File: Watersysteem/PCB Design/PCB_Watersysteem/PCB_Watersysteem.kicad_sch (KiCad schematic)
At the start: 69 parts, among them J1 12V ingang, J10 LED Water Level, J11 LED Nutrient Level, J12 Height Nutrients, J13 Height Mixer, J2 TTL Connector, J23 ReferentieProbe, J24 Voedingsstoffen 1, J25 Voedingsstoffen 2, J26 Voedingsstoffen 3, J6 Height Water, J7 Endstop Lade0, J8 Endstop Lade1, J9 Endstop UV, SW1 EN, SW2 BOOT, U1 ESP32-WROOM-32D, U2 MP1584_Module, U3 AMS1117-3.3, U4 ADS1115IDGS, U5 MCP23017_SO

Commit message: Update PCB
Alle connecties gemaakt
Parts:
- removed TP5, TP6: TestPoint, TestPoint:TestPoint_Pad_D2.5mm, symbol Connector:TestPoint
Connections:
- net Nutr1: now also U4.4 (AIN0); no longer U4.5 (AIN1)
- net Nutr2: now also U4.5 (AIN1); no longer U4.6 (AIN2)
- net Nutr3: now also U4.6 (AIN2); no longer U4.7 (AIN3)
- net RELAY_AIR: now also U5.25 (GPA4); no longer U5.26 (GPA5)
- net RELAY_UV: now also U5.26 (GPA5); no longer U5.25 (GPA4)
- net Nutr0 renamed RefProbe
- net RefProbe: now also U4.7 (AIN3); no longer U4.4 (AIN0)
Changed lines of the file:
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@@
 	)
 	(junction
-		(at 74.93 177.8)
-		(diameter 0)
-		(color 0 0 0 0)
-	)
-	(junction
 		(at 92.71 133.35)
 		(diameter 0)
@@
 	)
 	(junction
-		(at 38.1 177.8)
-		(diameter 0)
-		(color 0 0 0 0)
-	)
-	(junction
 		(at 96.52 143.51)
 		(diameter 0)
@@
 	(wire
 		(pts
-			(xy 74.93 177.8) (xy 77.47 177.8)
-		)
-		(stroke
-			(width 0)
-			(type default)
-		)
-	)
-	(wire
-		(pts
 			(xy 82.55 177.8) (xy 77.47 177.8)
 		)
@@
 	(wire
 		(pts
-			(xy 33.02 177.8) (xy 38.1 177.8)
-		)
-		(stroke
-			(width 0)
-			(type default)
-		)
-	)
-	(wire
-		(pts
 			(xy 234.95 123.19) (xy 250.19 123.19)
 		)
@@
 	(wire
 		(pts
-			(xy 38.1 177.8) (xy 44.45 177.8)
+			(xy 33.02 177.8) (xy 44.45 177.8)
 		)
 		(stroke
@@
 	(wire
 		(pts
-			(xy 72.39 177.8) (xy 74.93 177.8)
+			(xy 72.39 177.8) (xy 77.47 177.8)
 		)
 		(stroke
@@
 	(global_label "Nutr2"
 		(shape input)
-		(at 241.3 59.69 180)
+		(at 241.3 57.15 180)
 		(fields_autoplaced yes)
 		(effects
@@
 		)
 		(property "Intersheetrefs" "${INTERSHEET_REFS}"
-			(at 233.1139 59.69 0)
+			(at 233.1139 57.15 0)
 			(effects
 				(font
@@
 	(global_label "Nutr3"
 		(shape input)
-		(at 241.3 62.23 180)
+		(at 241.3 59.69 180)
 		(fields_autoplaced yes)
 		(effects
@@
 		)
 		(property "Intersheetrefs" "${INTERSHEET_REFS}"
-			(at 233.1139 62.23 0)
+			(at 233.1139 59.69 0)
 			(effects
 				(font
@@
 		)
 	)
-	(global_label "Nutr0"
+	(global_label "RefProbe"
 		(shape input)
-		(at 241.3 54.61 180)
+		(at 241.3 62.23 180)
 		(fields_autoplaced yes)
 		(effects
@@
 		)
 		(property "Intersheetrefs" "${INTERSHEET_REFS}"
-			(at 233.1139 54.61 0)
+			(at 229.7877 62.23 0)
 			(effects
 				(font
@@
 	(global_label "RELAY_AIR"
 		(shape input)
-		(at 139.7 140.97 0)
+		(at 139.7 138.43 0)
 		(fields_autoplaced yes)
 		(effects
@@
 		)
 		(property "Intersheetrefs" "${INTERSHEET_REFS}"
-			(at 152.2405 140.97 0)
+			(at 152.2405 138.43 0)
 			(effects
 				(font
@@
 		)
 	)
-	(global_label "Nutr0"
+	(global_label "RefProbe"
 		(shape input)
 		(at 190.5 50.8 0)
@@
 		)
 		(property "Intersheetrefs" "${INTERSHEET_REFS}"
-			(at 198.6861 50.8 0)
+			(at 202.0123 50.8 0)
 			(effects
 				(font
@@
 	(global_label "RELAY_UV"
 		(shape input)
-		(at 139.7 138.43 0)
+		(at 139.7 140.97 0)
 		(fields_autoplaced yes)
 		(effects
@@
 		)
 		(property "Intersheetrefs" "${INTERSHEET_REFS}"
-			(at 151.6962 138.43 0)
+			(at 151.6962 140.97 0)
 			(effects
 				(font
@@
 	(global_label "Nutr1"
 		(shape input)
-		(at 241.3 57.15 180)
+		(at 241.3 54.61 180)
 		(fields_autoplaced yes)
 		(effects
@@
 		)
 		(property "Intersheetrefs" "${INTERSHEET_REFS}"
-			(at 233.1139 57.15 0)
+			(at 233.1139 54.61 0)
 			(effects
 				(font
@@
 	)
 	(symbol
-		(lib_id "Connector:TestPoint")
-		(at 38.1 177.8 0)
-		(unit 1)
-		(exclude_from_sim no)
-		(in_bom yes)
-		(on_board yes)
-		(dnp no)
-		(fields_autoplaced yes)
-		(property "Reference" "TP5"
-			(at 40.64 173.2279 0)
-			(effects
-				(font
-					(size 1.27 1.27)
-				)
-				(justify left)
-			)
-		)
-		(property "Value" "TestPoint"
-			(at 40.64 175.7679 0)
-			(effects
-				(font
-					(size 1.27 1.27)
-				)
-				(justify left)
-			)
-		)
-		(property "Footprint" "TestPoint:TestPoint_Pad_D2.5mm"
-			(at 43.18 177.8 0)
-			(effects
-				(font
-					(size 1.27 1.27)
-				)
-				(hide yes)
-			)
-		)
-		(property "Datasheet" "~"
-			(at 43.18 177.8 0)
-			(effects
-				(font
-					(size 1.27 1.27)
-				)
-				(hide yes)
-			)
-		)
-		(property "Description" "test point"
-			(at 38.1 177.8 0)
-			(effects
-				(font
-					(size 1.27 1.27)
-				)
-				(hide yes)
-			)
-		)
-		(pin "1"
-		)
-		(instances
-			(project "PCB_Watersysteem"
-				(path "/de0b8b90-8fde-4ab1-b1b1-e85d44454ecd"
-					(reference "TP5")
-					(unit 1)
-				)
-			)
-		)
-	)
-	(symbol
 		(lib_id "power:GND")
 		(at 250.19 139.7 0)
@@
 					(unit 1)
 				)
-			)
-		)
-	)
-	(symbol
-		(lib_id "Connector:TestPoint")
-		(at 74.93 177.8 0)
-		(unit 1)
-		(exclude_from_sim no)
-		(in_bom yes)
-		(on_board yes)
-		(dnp no)
-		(fields_autoplaced yes)
-		(property "Reference" "TP6"
-			(at 77.47 173.2279 0)
-			(effects
-				(font
-					(size 1.27 1.27)
-				)
-				(justify left)
-			)
-		)
-		(property "Value" "TestPoint"
-			(at 77.47 175.7679 0)
-			(effects
-				(font
-					(size 1.27 1.27)
-				)
-				(justify left)
-			)
-		)
-		(property "Footprint" "TestPoint:TestPoint_Pad_D2.5mm"
-			(at 80.01 177.8 0)
-			(effects
-				(font
-					(size 1.27 1.27)
-				)
-				(hide yes)
-			)
-		)
-		(property "Datasheet" "~"
-			(at 80.01 177.8 0)
-			(effects
-				(font
-					(size 1.27 1.27)
-				)
-				(hide yes)
-			)
-		)
-		(property "Description" "test point"
-			(at 74.93 177.8 0)
-			(effects
-				(font
-					(size 1.27 1.27)
-				)
-				(hide yes)
-			)
-		)
-		(pin "1"
-		)
-		(instances
-			(project "PCB_Watersysteem"
-				(path "/de0b8b90-8fde-4ab1-b1b1-e85d44454ecd"
-					(reference "TP6")
-					(unit 1)
-				)

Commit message: Silkscreen
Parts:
- added J3: Conn_01x05_Pin, symbol Connector:Conn_01x05_Pin
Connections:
- net GND: now also J3.1 (Pin_1)
- net at U5.7 (GPB6): now also J3.3 (Pin_3)
- net at U5.8 (GPB7): now also J3.2 (Pin_2)
- no-connect marks 26 -> 23
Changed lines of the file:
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@@
 	)
 	(no_connect
-		(at 139.7 123.19)
-	)
-	(no_connect
 		(at 104.14 120.65)
 	)
@@
 	)
 	(no_connect
-		(at 139.7 120.65)
-	)
-	(no_connect
 		(at 33.02 50.8)
 	)
 	(no_connect
-		(at 139.7 118.11)
-	)
-	(no_connect
 		(at 33.02 76.2)
 	)
@@
 	(wire
 		(pts
+			(xy 139.7 123.19) (xy 157.48 123.19)
+		)
+		(stroke
+			(width 0)
+			(type default)
+		)
+	)
+	(wire
+		(pts
 			(xy 96.52 36.83) (xy 96.52 35.56)
 		)
@@
 	(wire
 		(pts
+			(xy 139.7 120.65) (xy 157.48 120.65)
+		)
+		(stroke
+			(width 0)
+			(type default)
+		)
+	)
+	(wire
+		(pts
 			(xy 50.8 177.8) (xy 53.34 177.8)
 		)
@@
 	)
 	(symbol
+		(lib_id "Connector:Conn_01x05_Pin")
+		(at 162.56 120.65 180)
+		(unit 1)
+		(exclude_from_sim no)
+		(in_bom yes)
+		(on_board yes)
+		(dnp no)
+		(fields_autoplaced yes)
+		(property "Reference" "J3"
+			(at 163.83 119.3799 0)
+			(effects
+				(font
+					(size 1.27 1.27)
+				)
+				(justify right)
+			)
+		)
+		(property "Value" "Conn_01x05_Pin"
+			(at 163.83 121.9199 0)
+			(effects
+				(font
+					(size 1.27 1.27)
+				)
+				(justify right)
+			)
+		)
+		(property "Footprint" ""
+			(at 162.56 120.65 0)
+			(effects
+				(font
+					(size 1.27 1.27)
+				)
+				(hide yes)
+			)
+		)
+		(property "Datasheet" "~"
+			(at 162.56 120.65 0)
+			(effects
+				(font
+					(size 1.27 1.27)
+				)
+				(hide yes)
+			)
+		)
+		(property "Description" "Generic connector, single row, 01x05, script generated"
+			(at 162.56 120.65 0)
+			(effects
+				(font
+					(size 1.27 1.27)
+				)
+				(hide yes)
+			)
+		)
+		(pin "3"
+		)
+		(pin "4"
+		)
+		(pin "2"
+		)
+		(pin "1"
+		)
+		(pin "5"
+		)
+		(instances
+			(project ""
+				(path "/de0b8b90-8fde-4ab1-b1b1-e85d44454ecd"
+					(reference "J3")
+					(unit 1)
+				)
+			)
+		)
+	)
+	(symbol
 		(lib_name "LED_1")
 		(lib_id "Device:LED")
@@
 					(unit 1)
 				)
+			)
+		)
+	)
+	(symbol
+		(lib_id "power:GND")
+		(at 157.48 125.73 0)
+		(unit 1)
+		(exclude_from_sim no)
+		(in_bom yes)
+		(on_board yes)
+		(dnp no)
+		(fields_autoplaced yes)
+		(property "Reference" "#PWR090"
+			(at 157.48 132.08 0)
+			(effects
+				(font
+					(size 1.27 1.27)
+				)
+				(hide yes)
+			)
+		)
+		(property "Value" "GND"
+			(at 157.48 130.81 0)
+			(effects
+				(font
+					(size 1.27 1.27)
+				)
+			)
+		)
+		(property "Footprint" ""
+			(at 157.48 125.73 0)
+			(effects
+				(font
+					(size 1.27 1.27)
+				)
+				(hide yes)
+			)
+		)
+		(property "Datasheet" ""
+			(at 157.48 125.73 0)
+			(effects
+				(font
+					(size 1.27 1.27)
+				)
+				(hide yes)
+			)
+		)
+		(property "Description" "Power symbol creates a global label with name \"GND\" , ground"
+			(at 157.48 125.73 0)
+			(effects
+				(font
+					(size 1.27 1.27)
+				)
+				(hide yes)
+			)
+		)
+		(pin "1"
+		)
+		(instances
+			(project "PCB_Watersysteem"
+				(path "/de0b8b90-8fde-4ab1-b1b1-e85d44454ecd"
+					(reference "#PWR090")
+					(unit 1)
+				)

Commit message: Afwerking
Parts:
- removed J3: Conn_01x05_Pin, symbol Connector:Conn_01x05_Pin
- removed TP15, TP7: TestPoint, TestPoint:TestPoint_Pad_D2.5mm, symbol Connector:TestPoint
- added J3: Backup GPIO, Connector_PinHeader_2.54mm:PinHeader_1x06_P2.54mm_Vertical, symbol Connector:Conn_01x06_Pin
- added J4: TestPins, Connector_PinHeader_2.54mm:PinHeader_1x02_P2.54mm_Vertical, symbol Connector:Conn_01x02_Pin
- TP1, TP2, TP3, TP4: footprint TestPoint:TestPoint_Pad_D2.5mm -> TestPoint:TestPoint_Pad_D2.0mm
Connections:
- net 3V3: now also J4.1 (Pin_1)
- net GND: now also J3.1 (Pin_1), J3.2 (Pin_2), J4.2 (Pin_2)
- net at U5.8 (GPB7): now also J3.3 (Pin_3)
- net at U5.7 (GPB6): now also J3.4 (Pin_4)
- net at U5.5 (GPB4): now also J3.6 (Pin_6)
- net at U5.6 (GPB5): now also J3.5 (Pin_5)
- no-connect marks 23 -> 22
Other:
- moved on the sheet: C14

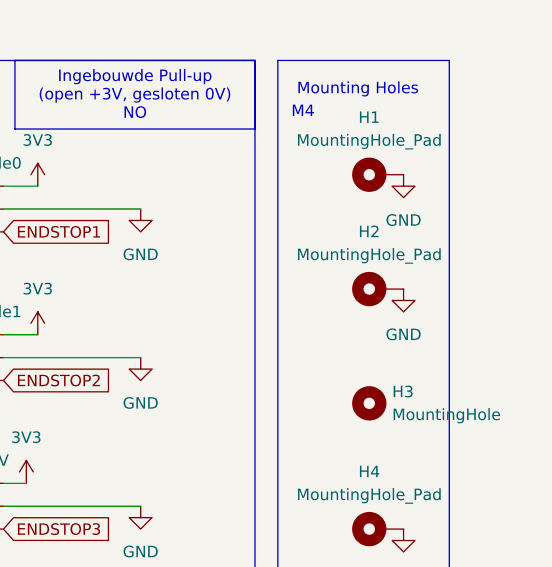
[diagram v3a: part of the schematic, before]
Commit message: PCB Update
samenbrengen designs, polarisaties plaatsen
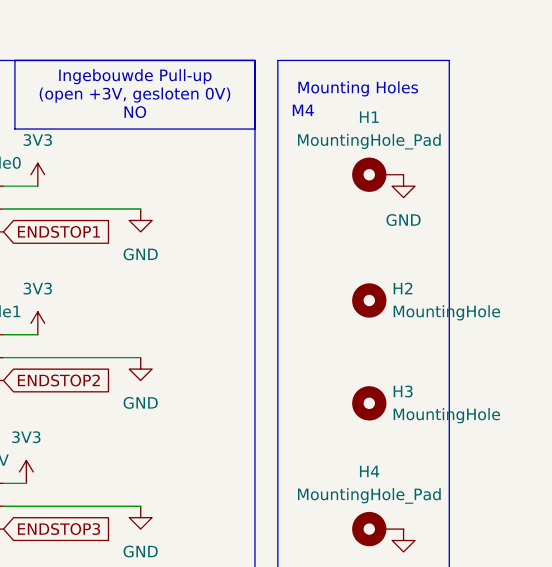
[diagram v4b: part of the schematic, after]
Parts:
- removed H2: MountingHole_Pad, MountingHole:MountingHole_3.2mm_M3_Pad_TopBottom, symbol Mechanical:MountingHole_Pad
- added H2: MountingHole, MountingHole:MountingHole_3.2mm_M3, symbol Mechanical:MountingHole
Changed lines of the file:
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@@
 	)
 	(symbol
+		(lib_id "Mechanical:MountingHole")
+		(at 275.59 133.35 0)
+		(unit 1)
+		(exclude_from_sim no)
+		(in_bom yes)
+		(on_board yes)
+		(dnp no)
+		(fields_autoplaced yes)
+		(property "Reference" "H2"
+			(at 278.13 132.0799 0)
+			(effects
+				(font
+					(size 1.27 1.27)
+				)
+				(justify left)
+			)
+		)
+		(property "Value" "MountingHole"
+			(at 278.13 134.6199 0)
+			(effects
+				(font
+					(size 1.27 1.27)
+				)
+				(justify left)
+			)
+		)
+		(property "Footprint" "MountingHole:MountingHole_3.2mm_M3"
+			(at 275.59 133.35 0)
+			(effects
+				(font
+					(size 1.27 1.27)
+				)
+				(hide yes)
+			)
+		)
+		(property "Datasheet" "~"
+			(at 275.59 133.35 0)
+			(effects
+				(font
+					(size 1.27 1.27)
+				)
+				(hide yes)
+			)
+		)
+		(property "Description" "Mounting Hole without connection"
+			(at 275.59 133.35 0)
+			(effects
+				(font
+					(size 1.27 1.27)
+				)
+				(hide yes)
+			)
+		)
+		(instances
+			(project "PCB_Watersysteem"
+				(path "/de0b8b90-8fde-4ab1-b1b1-e85d44454ecd"
+					(reference "H2")
+					(unit 1)
+				)
+			)
+		)
+	)
+	(symbol
 		(lib_id "power:GND")
 		(at 130.81 82.55 0)
@@
 	(symbol
 		(lib_id "power:GND")
-		(at 279.4 132.08 0)
-		(unit 1)
-		(exclude_from_sim no)
-		(in_bom yes)
-		(on_board yes)
-		(dnp no)
-		(fields_autoplaced yes)
-		(property "Reference" "#PWR031"
-			(at 279.4 138.43 0)
-			(effects
-				(font
-					(size 1.27 1.27)
-				)
-				(hide yes)
-			)
-		)
-		(property "Value" "GND"
-			(at 279.4 137.16 0)
-			(effects
-				(font
-					(size 1.27 1.27)
-				)
-			)
-		)
-		(property "Footprint" ""
-			(at 279.4 132.08 0)
-			(effects
-				(font
-					(size 1.27 1.27)
-				)
-				(hide yes)
-			)
-		)
-		(property "Datasheet" ""
-			(at 279.4 132.08 0)
-			(effects
-				(font
-					(size 1.27 1.27)
-				)
-				(hide yes)
-			)
-		)
-		(property "Description" "Power symbol creates a global label with name \"GND\" , ground"
-			(at 279.4 132.08 0)
-			(effects
-				(font
-					(size 1.27 1.27)
-				)
-				(hide yes)
-			)
-		)
-		(pin "1"
-		)
-		(instances
-			(project "PCB_Watersysteem"
-				(path "/de0b8b90-8fde-4ab1-b1b1-e85d44454ecd"
-					(reference "#PWR031")
-					(unit 1)
-				)
-			)
-		)
-	)
-	(symbol
-		(lib_id "power:GND")
 		(at 64.77 148.59 0)
 		(unit 1)
@@
 					(unit 1)
 				)
-			)
-		)
-	)
-	(symbol
-		(lib_id "Mechanical:MountingHole_Pad")
-		(at 276.86 132.08 90)
-		(unit 1)
-		(exclude_from_sim no)
-		(in_bom yes)
-		(on_board yes)
-		(dnp no)
-		(fields_autoplaced yes)
-		(property "Reference" "H2"
-			(at 275.59 125.73 90)
-			(effects
-				(font
-					(size 1.27 1.27)
-				)
-			)
-		)
-		(property "Value" "MountingHole_Pad"
-			(at 275.59 128.27 90)
-			(effects
-				(font
-					(size 1.27 1.27)
-				)
-			)
-		)
-		(property "Footprint" "MountingHole:MountingHole_3.2mm_M3_Pad_TopBottom"
-			(at 276.86 132.08 0)
-			(effects
-				(font
-					(size 1.27 1.27)
-				)
-				(hide yes)
-			)
-		)
-		(property "Datasheet" "~"
-			(at 276.86 132.08 0)
-			(effects
-				(font
-					(size 1.27 1.27)
-				)
-				(hide yes)
-			)
-		)
-		(property "Description" "Mounting Hole with connection"
-			(at 276.86 132.08 0)
-			(effects
-				(font
-					(size 1.27 1.27)
-				)
-				(hide yes)
-			)
-		)
-		(pin "1"
-		)
-		(instances
-			(project "PCB_Watersysteem"
-				(path "/de0b8b90-8fde-4ab1-b1b1-e85d44454ecd"
-					(reference "H2")
-					(unit 1)
-				)

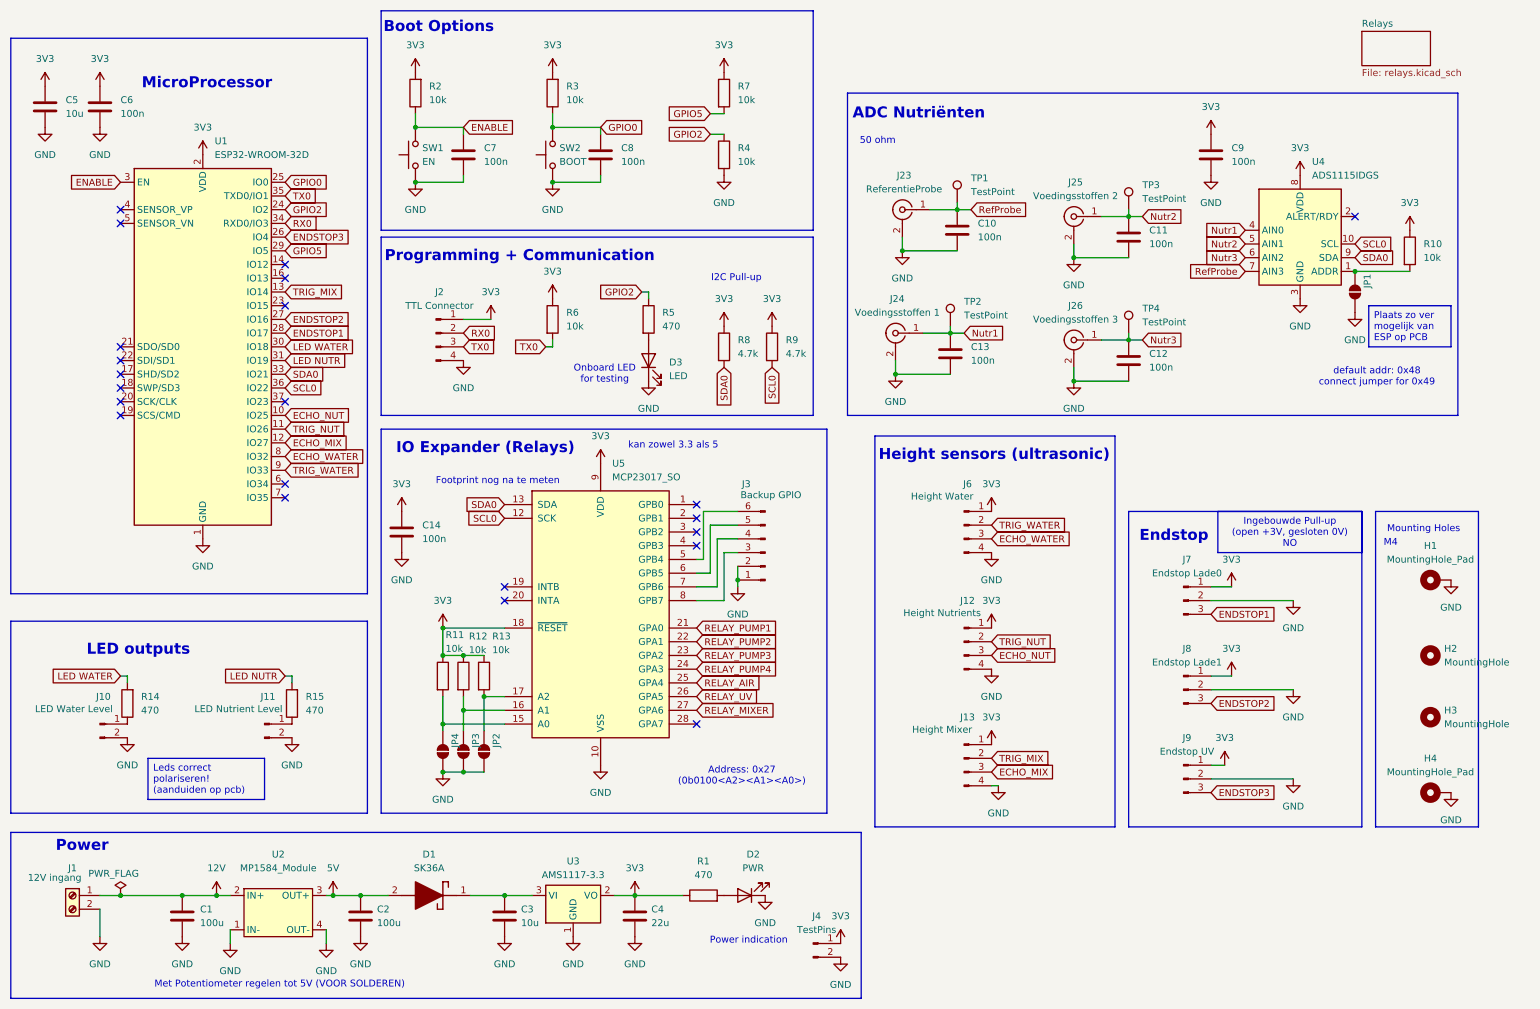
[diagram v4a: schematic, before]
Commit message: Update PCB
Afmetingen verkleind (100x100), rerouting, clean-up
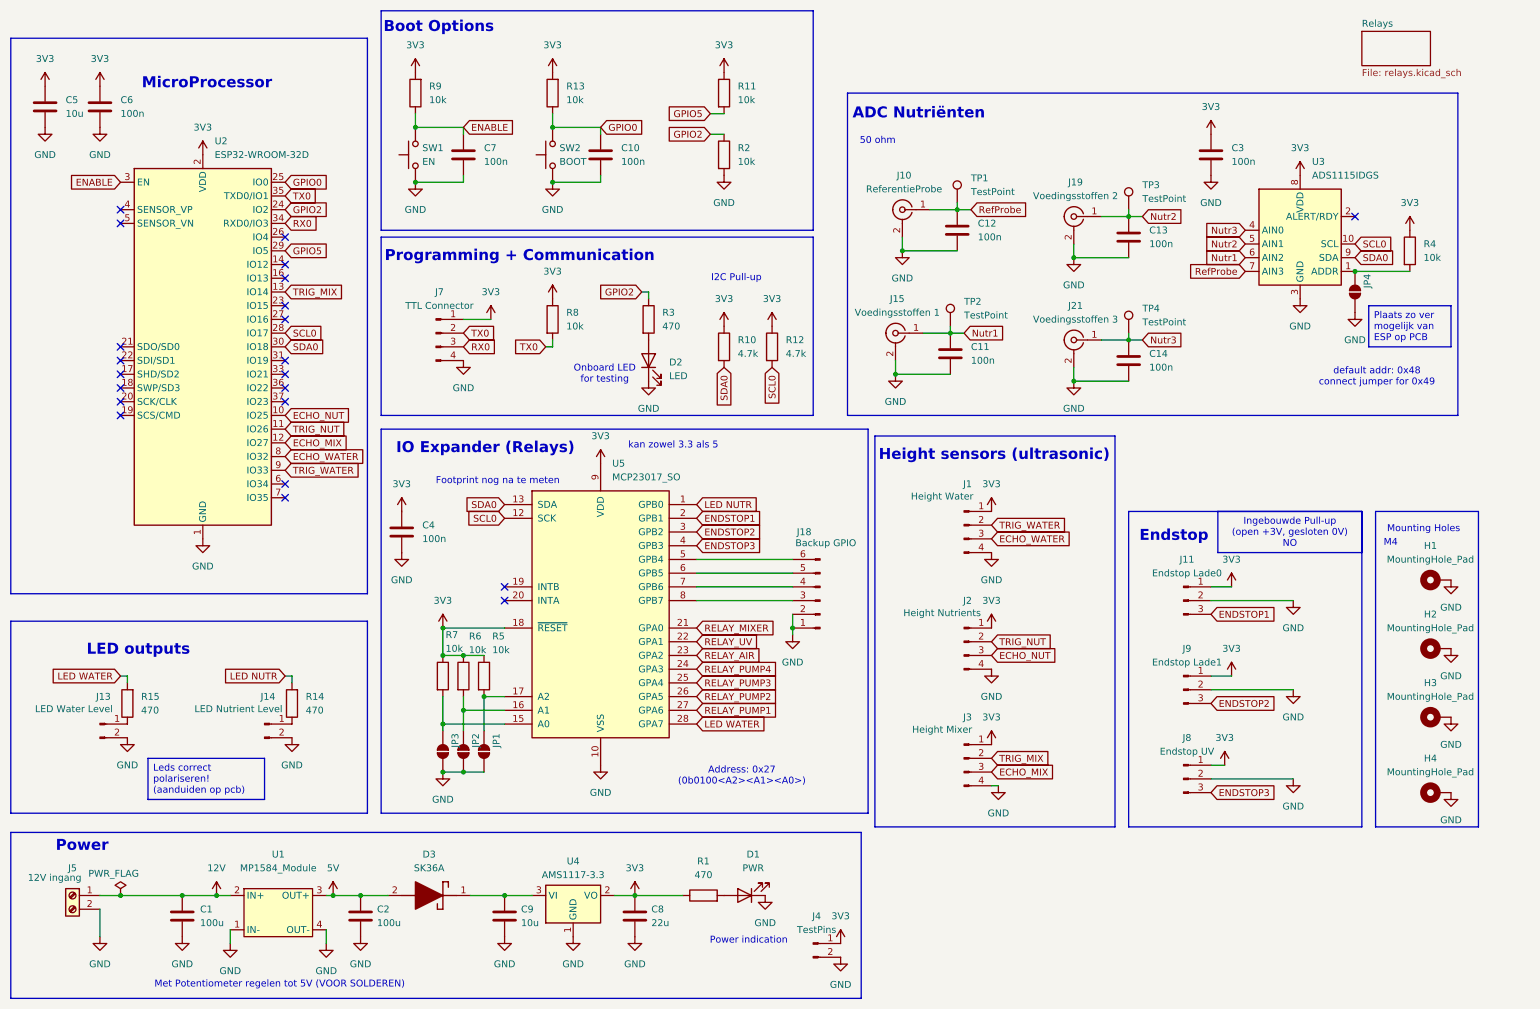
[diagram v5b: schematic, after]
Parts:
- removed H2, H3: MountingHole, MountingHole:MountingHole_3.2mm_M3, symbol Mechanical:MountingHole
- added H2, H3: MountingHole_Pad, MountingHole:MountingHole_3.2mm_M3_Pad_TopBottom, symbol Mechanical:MountingHole_Pad
- renumbered C8 to C10, C13 to C11, C10 to C12, C11 to C13, C12 to C14, C9 to C3, C14 to C4, C4 to C8, C3 to C9, D2 to D1, D3 to D2, D1 to D3, J6 to J1, J23 to J10, J7 to J11, J10 to J13, J11 to J14, J24 to J15, J3 to J18, J25 to J19, J12 to J2, J26 to J21, J13 to J3, J1 to J5, J2 to J7, J9 to J8, J8 to J9, JP2 to JP1, JP3 to JP2, JP4 to JP3, JP1 to JP4, R8 to R10, R7 to R11, R9 to R12, R3 to R13, R15 to R14, R14 to R15, R4 to R2, R5 to R3, R10 to R4, R13 to R5, R12 to R6, R11 to R7, R6 to R8, R2 to R9, U2 to U1, U1 to U2, U4 to U3, U3 to U4
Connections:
- net ENDSTOP1: now also U5.2 (GPB1); no longer U2.28 (IO17)
- net ENDSTOP2: now also U5.3 (GPB2); no longer U2.27 (IO16)
- net ENDSTOP3: now also U5.4 (GPB3); no longer U2.26 (IO4)
- net GND: now also H2.1, H3.1
- net LED NUTR: now also U5.1 (GPB0); no longer U2.31 (IO19)
- net LED WATER: now also U5.28 (GPA7); no longer U2.30 (IO18)
- net Nutr1: now also U3.6 (AIN2); no longer U3.4 (AIN0)
- net Nutr3: now also U3.4 (AIN0); no longer U3.6 (AIN2)
- net RELAY_AIR: now also U5.23 (GPA2); no longer U5.25 (GPA4)
- net RELAY_MIXER: now also U5.21 (GPA0); no longer U5.27 (GPA6)
- net RELAY_PUMP1: now also U5.27 (GPA6); no longer U5.21 (GPA0)
- net RELAY_PUMP2: now also U5.26 (GPA5); no longer U5.22 (GPA1)
- net RELAY_PUMP3: now also U5.25 (GPA4); no longer U5.23 (GPA2)
- net RELAY_UV: now also U5.22 (GPA1); no longer U5.26 (GPA5)
- net RX0: now also J7.3 (Pin_3); no longer J7.2 (Pin_2)
- net SCL0: now also U2.28 (IO17); no longer U2.36 (IO22)
- net SDA0: now also U2.30 (IO18); no longer U2.33 (IO21)
- net TX0: now also J7.2 (Pin_2); no longer J7.3 (Pin_3)
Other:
- moved on the sheet: J18
